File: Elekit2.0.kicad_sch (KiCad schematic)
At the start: 43 parts, among them Q1 AO3401A, Q2 2N7002, SW1 SW_Push, U1 TYPE-C_16PIN_2MD(073), U2 74HC595, U3 MY-2032-12, U4 MY-2032-12, U5 XC6206P332MR, U6 TS-1187A-B-A-B, U7 ESP32-C3-WROOM-02-N4(4MB), U8 TS-1187A-B-A-B, U9 SRV05-4-P-T7

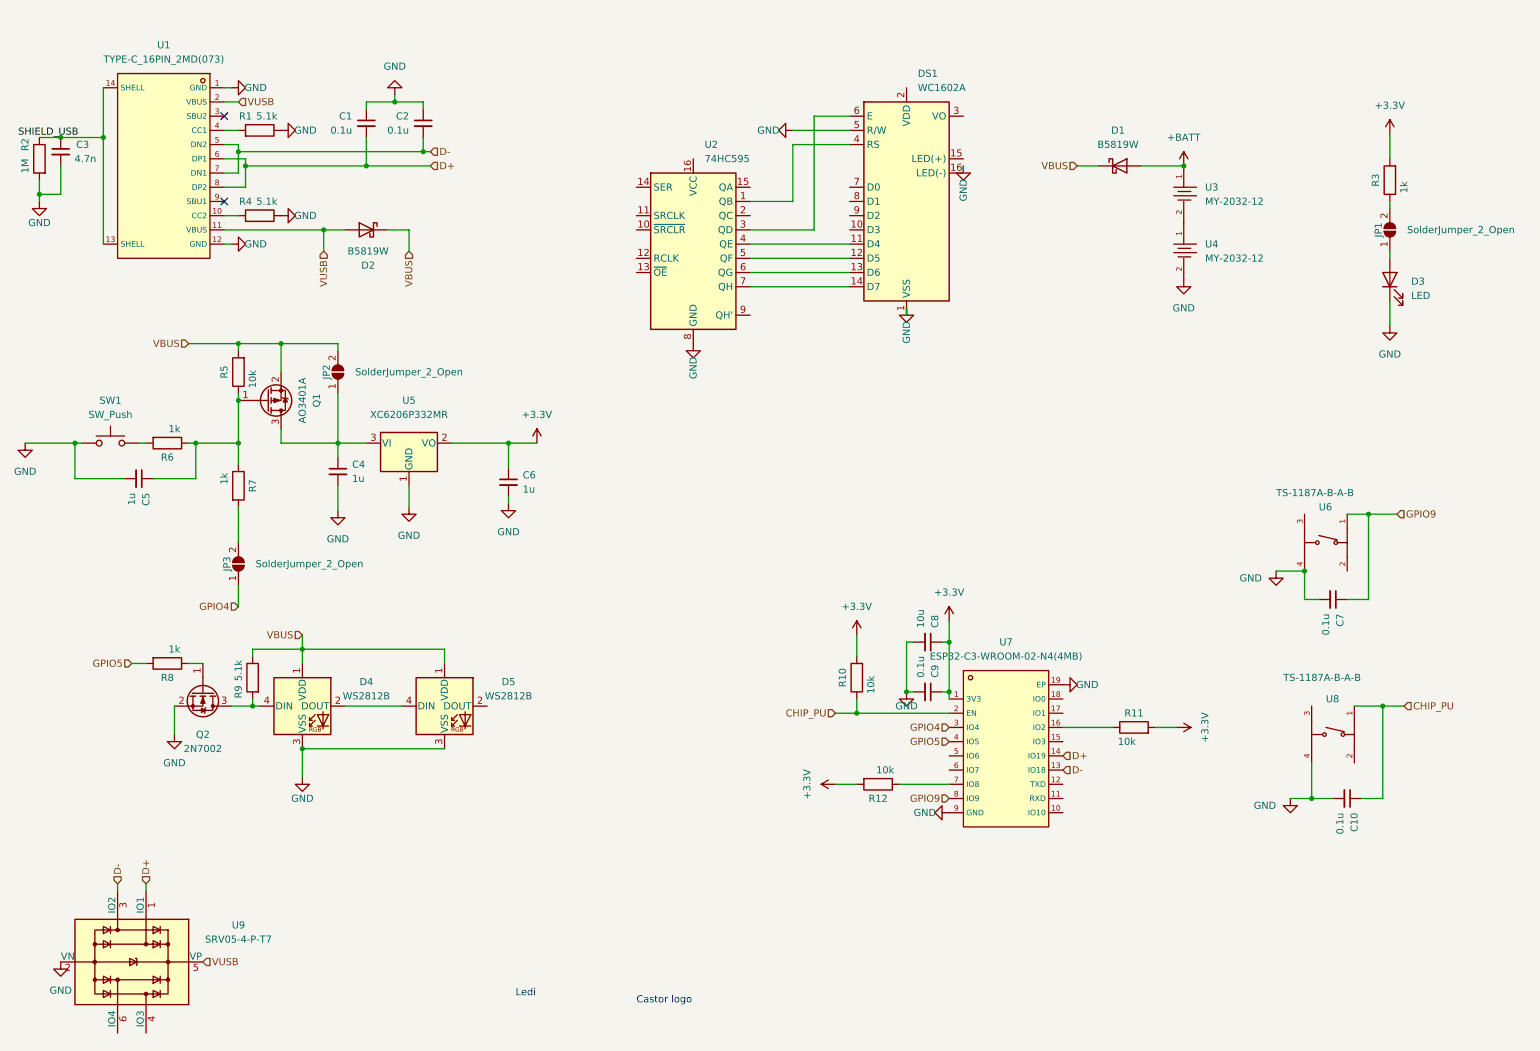
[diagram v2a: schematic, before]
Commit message: Update libraries. Finish LCD connector. save before changing LDO
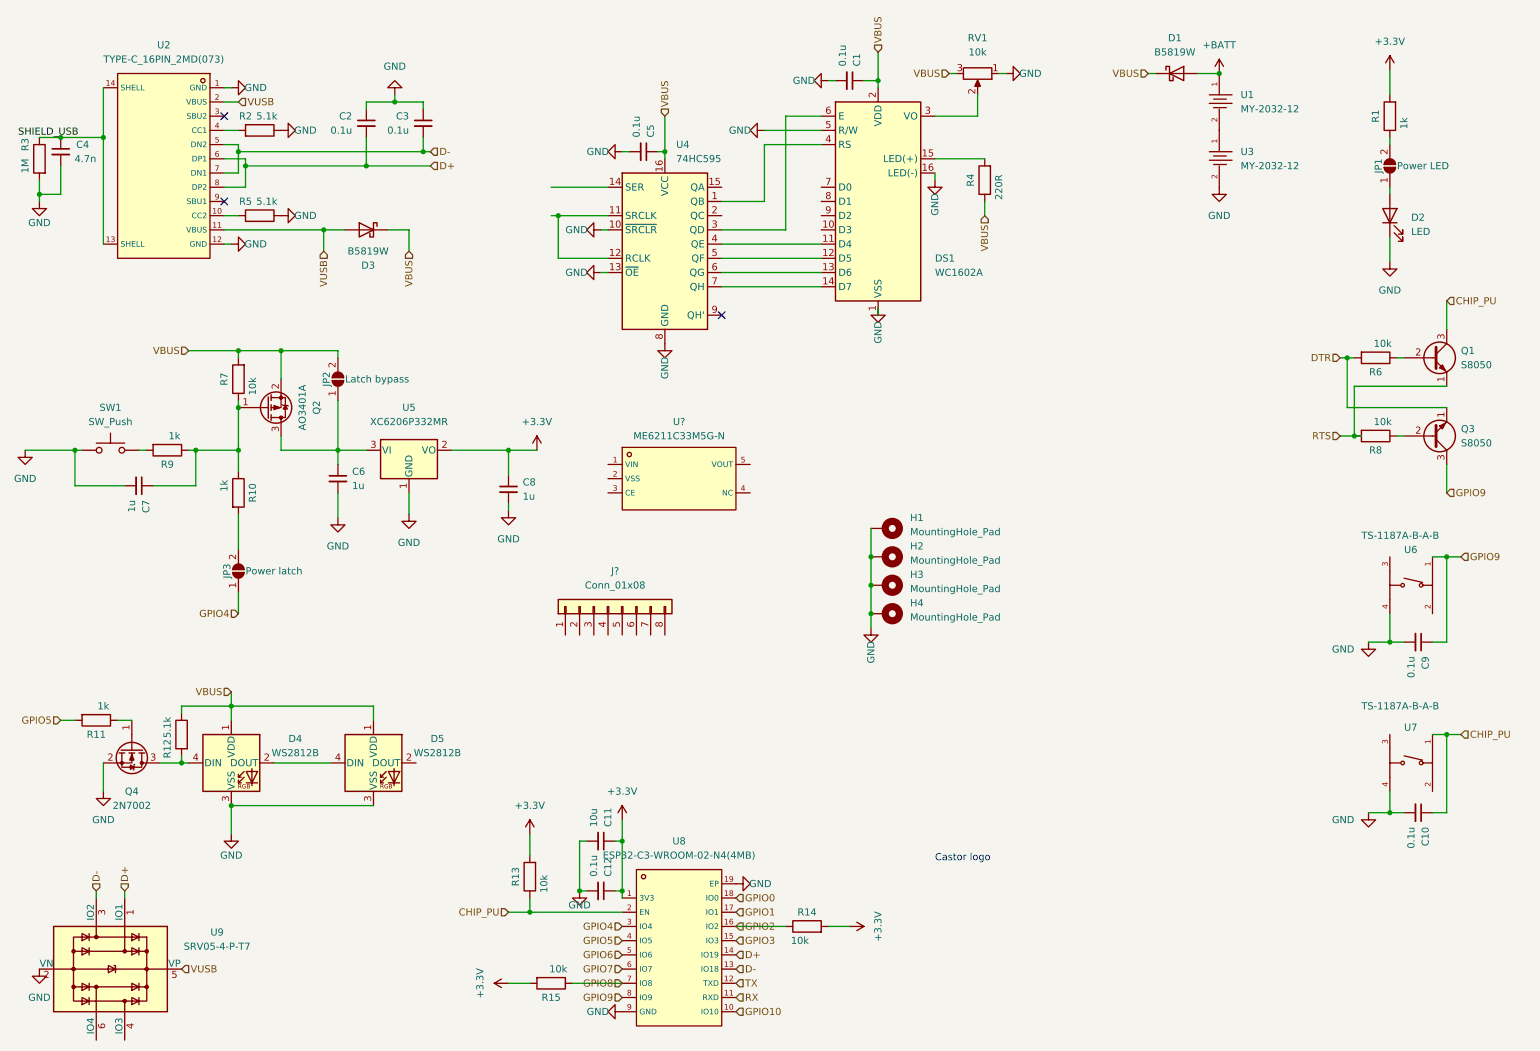
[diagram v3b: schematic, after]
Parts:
- added C1, C5: 0.1u, Capacitor_SMD:C_0805_2012Metric, symbol Device:C_Small
- added H1, H2, H3, H4: MountingHole_Pad, MountingHole:MountingHole_3.2mm_M3_Pad_Via, symbol Mechanical:MountingHole_Pad
- added J?: Conn_01x08, symbol Connector_Generic:Conn_01x08
- added Q1, Q3: S8050, Package_TO_SOT_THT:TO-92_Inline, symbol Transistor_BJT:S8050
- added R4: 220R, Resistor_SMD:R_0805_2012Metric, symbol Device:R
- added R6, R8: 10k, Resistor_SMD:R_1206_3216Metric, symbol Device:R
- added RV1: 10k, Potentiometer_THT:Potentiometer_Bourns_3296W_Vertical, symbol Device:R_Potentiometer
- added U?: ME6211C33M5G-N, 0_JLCPCB_Footprints:SOT-23-5_L3.0-W1.7-P0.95-LS2.8-BR, symbol 0_JLCPCB_Symbols:ME6211C33M5G-N
- DS1: now left out of the parts list
- JP1: value SolderJumper_2_Open -> Power LED; now left out of the parts list
- JP2: value SolderJumper_2_Open -> Latch bypass; now left out of the parts list
- JP3: value SolderJumper_2_Open -> Power latch; now left out of the parts list
- U4: renamed from U2; LCSC (none) -> C5947
- renumbered C8 to C11, C9 to C12, C1 to C2, C2 to C3, C3 to C4, C4 to C6, C5 to C7, C6 to C8, C7 to C9, D3 to D2, D2 to D3, Q1 to Q2, Q2 to Q4, R3 to R1, R7 to R10, R8 to R11, R9 to R12, R10 to R13, R11 to R14, R12 to R15, R1 to R2, R2 to R3, R4 to R5, R5 to R7, R6 to R9, U3 to U1, U1 to U2, U4 to U3, U8 to U7, U7 to U8
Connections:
- net CHIP_PU: now also Q1.3 (C)
- net GND: now also U4.10 (~{SRCLR}), U4.13 (~{OE}), C1.2, C5.2, H1.1, H2.1, H3.1, H4.1, RV1.1
- net GPIO9: now also Q3.3 (C)
- net VBUS: now also DS1.2 (VDD), U4.16 (VCC), C1.1, C5.1, R4.1, RV1.3
- net GPIO10: now reaches U8.10 (IO10)
- net RX: now reaches U8.11 (RXD)
- net TX: now reaches U8.12 (TXD)
- net GPIO3: now reaches U8.15 (IO3)
- net GPIO2: now reaches R14.1, U8.16 (IO2)
- net GPIO1: now reaches U8.17 (IO1)
- net GPIO0: now reaches U8.18 (IO0)
- net GPIO6: now reaches U8.5 (IO6)
- net GPIO7: now reaches U8.6 (IO7)
- net GPIO8: now reaches R15.1, U8.7 (IO8)
- net at DS1.15 (LED(+)): now also R4.2
- net at DS1.3 (VO): now also RV1.2
- net at U4.11 (SRCLK): now also U4.12 (RCLK)
- new net: Q3.2 (B), R8.1
- new net: Q1.2 (B), R6.1
- new net DTR: Q3.1 (E), R6.2
- new net RTS: Q1.1 (E), R8.2
- no-connect marks 2 -> 3
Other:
- note removed: "Ledi"
- moved on the sheet: C10, C11, C12, C6, C7, C8, C9, D1, D2, D4, D5, DS1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

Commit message: Add H bridge motor controllers and create first draft of pcb
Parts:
- removed C6, C7: 1u, Capacitor_SMD:C_0805_2012Metric, symbol Device:C_Small
- removed D1, D3: B5819W, Diode_SMD:D_SOD-123, symbol Diode:1N5820
- removed D2: LED, LED_SMD:LED_0805_2012Metric, symbol Device:LED
- removed Q1, Q3: S8050, Package_TO_SOT_THT:TO-92_Inline, symbol Transistor_BJT:S8050
- removed Q2: AO3401A, Package_TO_SOT_SMD:SOT-23, symbol Transistor_FET:AO3401A
- removed R10: 1k, Resistor_SMD:R_0805_2012Metric, symbol Device:R
- removed R2: 5.1k, Resistor_SMD:R_0805_2012Metric, symbol Device:R
- removed R3: 1M, Resistor_SMD:R_1206_3216Metric, symbol Device:R
- removed U2: TYPE-C_16PIN_2MD(073), 0_JLCPCB_Footprints:USB-C-SMD_TYPE-C-6PIN-2MD-073, symbol 0_JLCPCB_Symbols:TYPE-C_16PIN_2MD(073)
- removed U5: XC6206P332MR, Package_TO_SOT_SMD:SOT-23, symbol Regulator_Linear:XC6206PxxxMR
- added C1: 0.1u 50V, Capacitor_SMD:C_0402_1005Metric, symbol Device:C_Small
- added C10: 1u, Capacitor_SMD:C_0805_2012Metric, symbol Device:C_Small
- added C14, C16, C17, C18, C20, C21, C22, C5: 0.1u, Capacitor_SMD:C_0805_2012Metric, symbol Device:C_Small
- added C19, C23: 10u 50V, Capacitor_SMD:C_1206_3216Metric, symbol Device:C_Small
- added C9: 1u 25V, Capacitor_SMD:C_0402_1005Metric, symbol Device:C_Small
- added D1, D2, D3, D5, D8: SS34, Diode_SMD:D_SMA, symbol Device:D_Schottky
- added D11, D12: WS2812B, LED_SMD:LED_WS2812B_PLCC4_5.0x5.0mm_P3.2mm, symbol LED:WS2812B
- added D4: LED, LED_SMD:LED_0805_2012Metric, symbol Device:LED
- added D6, D7: 1N4148W, Diode_SMD:D_SOD-123, symbol Diode:1N4148W
- added J1, J2, J3, J4: Screw_Terminal_01x02, 0_JLCPCB_Footprints:CONN-TH_P5.00_KF301-5.0-2P, symbol Connector:Screw_Terminal_01x02
- added J10, J5, J9: Conn_01x03_Male, Connector_PinHeader_2.54mm:PinHeader_1x03_P2.54mm_Vertical, symbol Connector:Conn_01x03_Male
- added J11: DS18B20 temperature sensor, Connector_PinHeader_2.54mm:PinHeader_1x03_P2.54mm_Vertical, symbol Connector:Conn_01x03_Male
- added J12, J13: Conn_01x01_Male, 0_JLCPCB_Footprints:PinHeader_1x01_P2.54mm_Vertical, symbol Connector:Conn_01x01_Male
- added J6: Conn_01x06_Male, Connector_PinHeader_2.54mm:PinHeader_1x06_P2.54mm_Vertical, symbol Connector:Conn_01x06_Male
- added J8: Conn_01x08, Connector_PinHeader_2.54mm:PinHeader_1x08_P2.54mm_Vertical, symbol Connector_Generic:Conn_01x08
- added JP4: Power LED, Jumper:SolderJumper-2_P1.3mm_Open_RoundedPad1.0x1.5mm, symbol Jumper:SolderJumper_2_Open
- added JP5, JP6, JP7, JP8, JP9: led bypass, Jumper:SolderJumper-2_P1.3mm_Open_RoundedPad1.0x1.5mm, symbol Jumper:SolderJumper_2_Open
- added LOGO1: CASTOR, 0_JLCPCB_Footprints:Castor logo, symbol 0_JLCPCB_Symbols:CASTOR
- added Q1, Q3: 2N7002, Package_TO_SOT_SMD:SOT-23, symbol Transistor_FET:2N7002
- added R1: 1M, Resistor_SMD:R_1206_3216Metric, symbol Device:R
- added R13, R14: 1k, Resistor_SMD:R_0805_2012Metric, symbol Device:R
- added R16: 4.7k, Resistor_SMD:R_0805_2012Metric, symbol Device:R
- added R18, R4: 10k, Resistor_SMD:R_0805_2012Metric, symbol Device:R
- added R19, R21: 0R, Resistor_SMD:R_1206_3216Metric, symbol Device:R
- added SW2, SW3, SW4, SW5, SW6: SW_Push, Button_Switch_THT:SW_PUSH_6mm, symbol Switch:SW_Push
- added U1: MINI_5PTP, 0_JLCPCB_Footprints:MINI-USB-SMD_MINI-5PTP, symbol 0_JLCPCB_Symbols:MINI_5PTP
- added U11: DHT11, Sensor:Aosong_DHT11_5.5x12.0_P2.54mm, symbol Sensor:DHT11
- added U12, U15: DRV8870DDA, Package_SO:Texas_HTSOP-8-1EP_3.9x4.9mm_P1.27mm_EP2.95x4.9mm_Mask2.4x3.1mm_ThermalVias, symbol Driver_Motor:DRV8870DDA
- added U3: L7805, Package_TO_SOT_THT:TO-220-3_Vertical, symbol Regulator_Linear:L7805
- C2: value 0.1u -> 0.1u 50V; footprint Capacitor_SMD:C_0805_2012Metric -> Capacitor_SMD:C_0402_1005Metric; LCSC C28233 -> C307331
- C3: value 0.1u -> 4.7n; LCSC C28233 -> C1779
- C4: value 4.7n -> 0.47u 50v; LCSC C1779 -> C13967
- C8: value 1u -> 1u 25V; footprint Capacitor_SMD:C_0805_2012Metric -> Capacitor_SMD:C_0402_1005Metric; LCSC C28323 -> C52923
- H1, H2, H3, H4: footprint MountingHole:MountingHole_3.2mm_M3_Pad_Via -> MountingHole:MountingHole_3.2mm_M3; symbol Mechanical:MountingHole_Pad -> Mechanical:MountingHole; now in the parts list
- J7: renamed from J?; footprint (none) -> Connector_PinHeader_2.54mm:PinHeader_1x08_P2.54mm_Vertical
- JP1: value Power LED -> Latch bypass
- JP2: value Latch bypass -> VIN DIODE BYPASS
- JP3: value Power latch -> Latch control
- R2: renamed from R4; LCSC C17513 -> C17557
- R5: value 5.1k -> 1k; LCSC C27834 -> C17513
- R6: footprint Resistor_SMD:R_1206_3216Metric -> Resistor_SMD:R_0805_2012Metric; LCSC C4410 -> C17414
- R7: value 10k -> 1M; footprint Resistor_SMD:R_1206_3216Metric -> Resistor_SMD:R_0805_2012Metric; LCSC C4410 -> C17514
- R8: value 10k -> 1k; footprint Resistor_SMD:R_1206_3216Metric -> Resistor_SMD:R_0805_2012Metric; LCSC C4410 -> C17513
- gave numbers to parts that had none: 1
- renumbered C9 to C13, C10 to C15, C1 to C6, C5 to C7, D5 to D10, D4 to D9, Q4 to Q2, R11 to R10, R12 to R11, R13 to R12, R14 to R15, R15 to R17, R1 to R3, U7 to U10, U1 to U2, U3 to U4, U9 to U5, U4 to U6, U6 to U8, U8 to U9
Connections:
- net DTR is gone; now on net GND: R6.2
- net RTS is gone; now on net GPIO5: R8.2
- net +3.3V: now also C12.2, U7.5 (VOUT), C9.1, J11.3 (Pin_3), R16.1, R18.1, U11.1 (VCC), U12.4 (VREF), U15.4 (VREF); no longer C12.1, C8.1
- net +BATT: now also D1.2 (A)
- net D+: now also C1.1, U1.3 (D+); no longer C2.2
- net D-: now also C2.2, U5.6 (IO4), U1.2 (D-); no longer C3.2, U5.3 (IO2)
- net GND: now also C12.1, C3.2, C4.1, C8.1, R7.1, U7.2 (VSS), C1.2, C10.2, C14.1, C16.1, C17.1, C18.1, C19.2, C20.1, C21.1, C22.1, C23.2, C5.1, C9.2, D11.3 (VSS), D12.3 (VSS), J1.1 (Pin_1), J10.1 (Pin_1), J11.1 (Pin_1), J4.1 (Pin_1), J5.1 (Pin_1), J6.1 (Pin_1), J9.1 (Pin_1), JP4.1 (A), Q1.2 (S), Q3.2 (S), R1.2, R19.2, R21.2, SW2.1, SW3.1, SW4.1, SW5.1, SW6.1, U1.5 (GND), U11.4 (GND), U12.1 (GND), U12.9 (GND), U15.1 (GND), U15.9 (GND), U3.2 (GND); no longer C12.2, C3.1, C4.2, C8.2, H1.1, H2.1, H3.1, H4.1, R5.1, SW1.1
- net GPIO0: now also J7.1 (Pin_1)
- net GPIO1: now also J7.2 (Pin_2)
- net GPIO10: now also J8.3 (Pin_3)
- net GPIO2: now also J7.3 (Pin_3)
- net GPIO3: now also J7.4 (Pin_4)
- net GPIO4: now also J7.5 (Pin_5), JP3.2 (B); no longer JP3.1 (A)
- net GPIO5: now also J7.6 (Pin_6)
- net GPIO6: now also J7.7 (Pin_7), R13.2
- net GPIO7: now also J7.8 (Pin_8)
- net GPIO8: now also J8.1 (Pin_1)
- net GPIO9: now also J8.2 (Pin_2)
- net RX: now also J6.4 (Pin_4), J8.4 (Pin_4)
- net TX: now also J6.5 (Pin_5), J8.5 (Pin_5)
- net VBUS: now also C8.2, JP1.2 (B), JP2.1 (A), R9.1, SW1.2, U7.1 (VIN), D1.1 (K), D11.1 (VDD), D12.1 (VDD), D2.1 (K), D3.1 (K), D5.1 (K), D8.1 (K), J10.3 (Pin_3), J5.2 (Pin_2), J9.2 (Pin_2), R14.1; no longer JP2.2 (B), R7.2
- net VUSB: now also D3.2 (A), U1.1 (VCC)
- net at D9.4 (DIN), Q2.3 (D), R11.2: now also JP6.1 (A)
- net at D10.4 (DIN), D9.2 (DOUT): now also JP6.2 (B), JP7.1 (A)
- net EN_LDO: now reaches JP1.1 (A)
- net EN_LDO: now also R7.2, U7.3 (CE), D6.1 (K), D7.1 (K)
- net SERVO1: now reaches R9.2
- net SERVO1: now also J5.3 (Pin_3), Q1.3 (D); no longer SW1.2
- net at R5.2: now also JP3.1 (A)
- net at R8.1: now also Q1.1 (G)
- net at R3.1: now also D4.2 (A); no longer JP1.2 (B)
- net at D10.2 (DOUT): now also D11.4 (DIN), JP7.2 (B), JP8.1 (A)
- net BTN: now reaches R6.1
- net BTN: now also C10.1, D6.2 (A), R4.2
- new net: C14.2, SW2.2
- new net: D11.2 (DOUT), D12.4 (DIN), JP8.2 (B), JP9.1 (A)
- new net: D12.2 (DOUT), J10.2 (Pin_2), JP9.2 (B)
- new net: D5.2 (A), J4.2 (Pin_2), JP2.2 (B)
- new net: R4.1, SW1.1
- new net: C21.2, SW6.2
- new net: J13.1 (Pin_1), R19.1, U15.7 (ISEN)
- new net: J12.1 (Pin_1), R21.1, U12.7 (ISEN)
- new net: D4.1 (K), JP4.2 (B)
- new net: D7.2 (A), R5.1
- new net: C16.2, SW3.2
- new net: J6.3 (Pin_3), JP5.1 (A)
- new net: C3.1, R1.1, U1.6, U1.7, U1.8, U1.9
- new net: D8.2 (A), JP5.2 (B)
- new net: C17.2, SW4.2
- new net: Q3.1 (G), R13.1
- new net: C20.2, SW5.2
- new net: C5.2, D2.2 (A), U3.3 (OUT)
- new net A1: J2.1 (Pin_1), U15.6 (OUT1)
- new net A1_c: U15.3 (IN1)
- new net A2: J2.2 (Pin_2), U15.8 (OUT2)
- new net A2_C: U15.2 (IN2)
- new net B1: J3.1 (Pin_1), U12.6 (OUT1)
- new net B1_c: U12.3 (IN1)
- new net B2: J3.2 (Pin_2), U12.8 (OUT2)
- new net B2_C: U12.2 (IN2)
- new net DHT_DATA: R18.2, U11.2 (IO)
- new net DQ: J11.2 (Pin_2), R16.2
- new net HVBUS: C18.2, C19.1, C22.2, C23.1, C4.2, J1.2 (Pin_2), U12.5 (VM), U15.5 (VM), U3.1 (IN)
- new net SERVO2: J9.3 (Pin_3), Q3.3 (D), R14.2
- no-connect marks 3 -> 5
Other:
- note added: "BAT"
- note added: "ESP32"
- note added: "HVBUS"
- note added: "IO"
- note added: "LCD"
- note added: "USB"
- note added: "VBUS"
- note added: "WS2812B"
- note removed: "Castor logo"
- moved on the sheet: C11, C13, C15, C6, C7, D10, D9, DS1, J7, Q2, R10, R11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
